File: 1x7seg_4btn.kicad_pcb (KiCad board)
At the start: 2 copper layers, 53.7 x 26.3 mm, 49 parts, among them CON1 AVR-ISP, IC1 ATTINY88-A, Q1 2N7002, Q2 2N7002, Q3 2N7002, U1 74HC14D_653, U10 MC14543B, U2 SW_SPST, U3 SW_SPST, U6 SW_SPST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

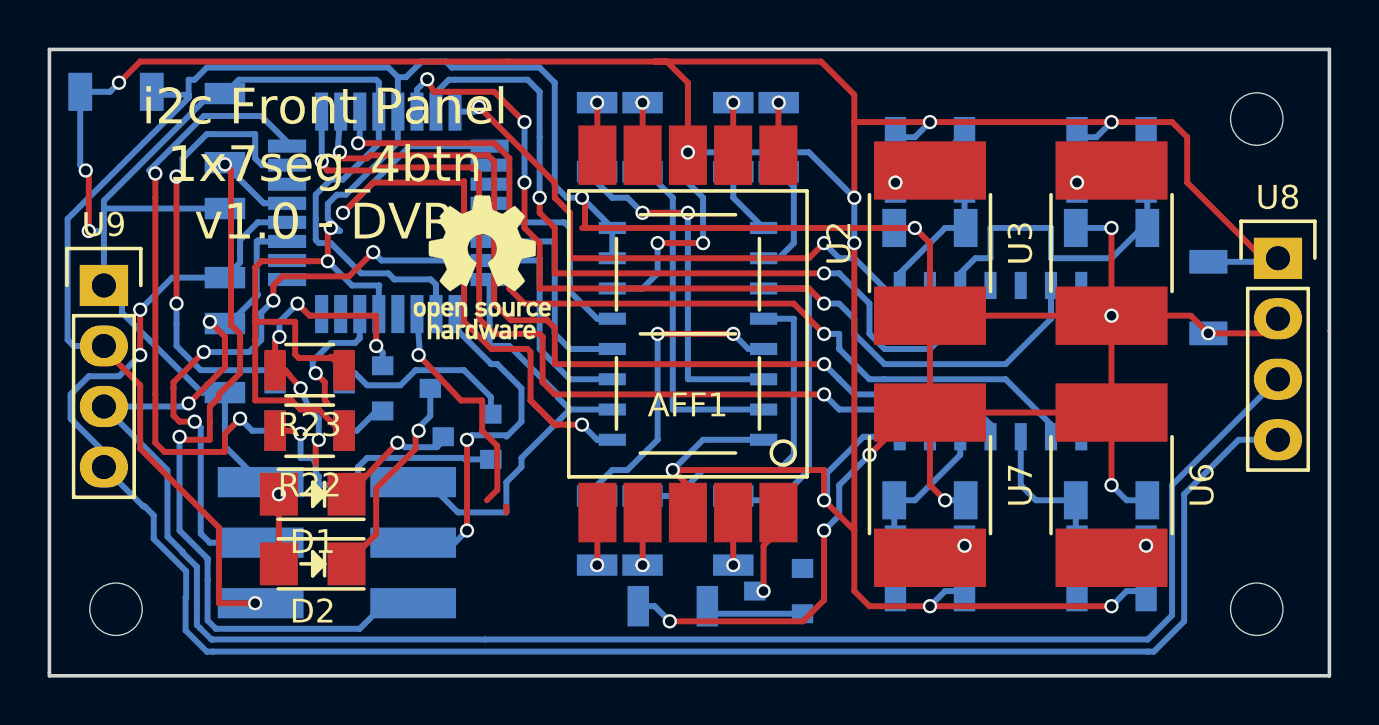
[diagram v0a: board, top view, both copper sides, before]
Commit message: Moved oshw logo
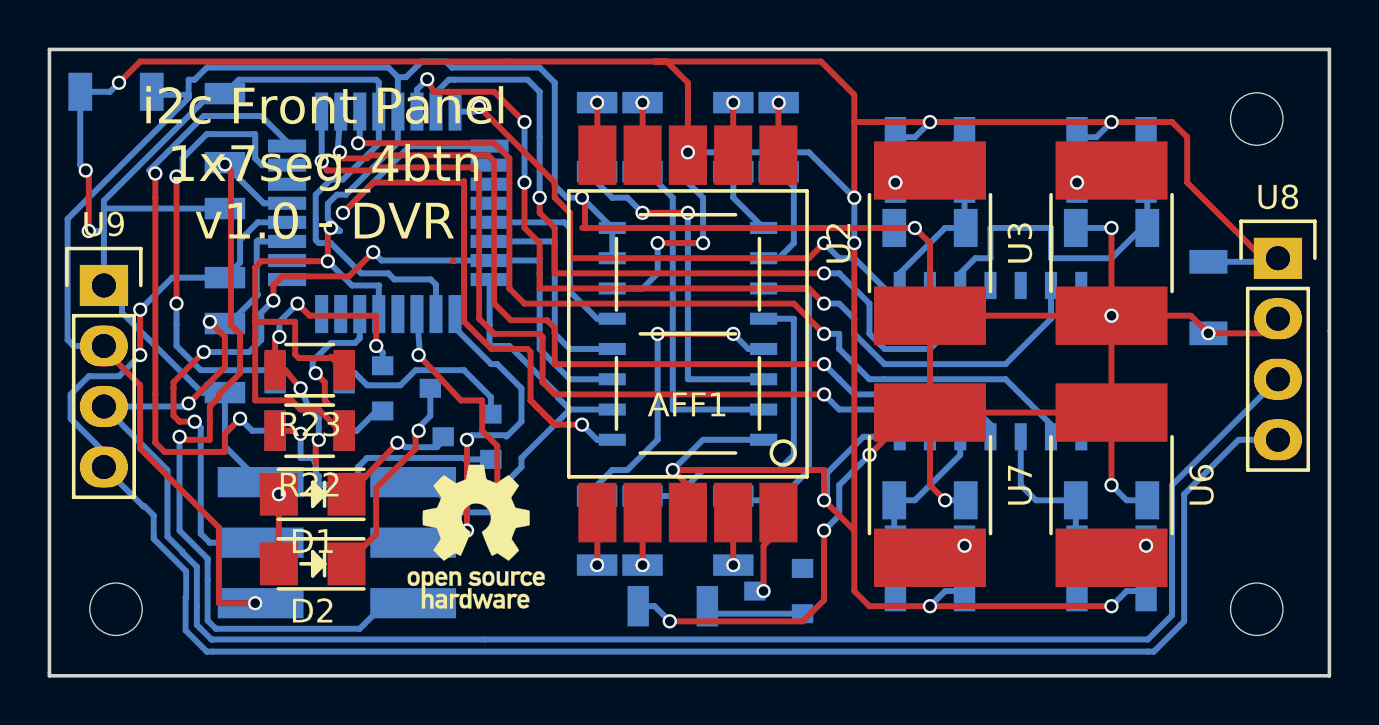
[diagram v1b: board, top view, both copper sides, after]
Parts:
- moved REF*** 11.3 mm to (50.7, 41.5)
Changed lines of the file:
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@@
   )
   (module Symbols:OSHW-Logo_5.7x6mm_SilkScreen (layer F.Cu)
-    (at 50.927 30.226)
+    (at 50.673 41.529)
     (descr "Open Source Hardware Logo")
     (tags "Logo OSHW")

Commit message: Moved header pins on 1x7seg_4btn version to match height on both sides
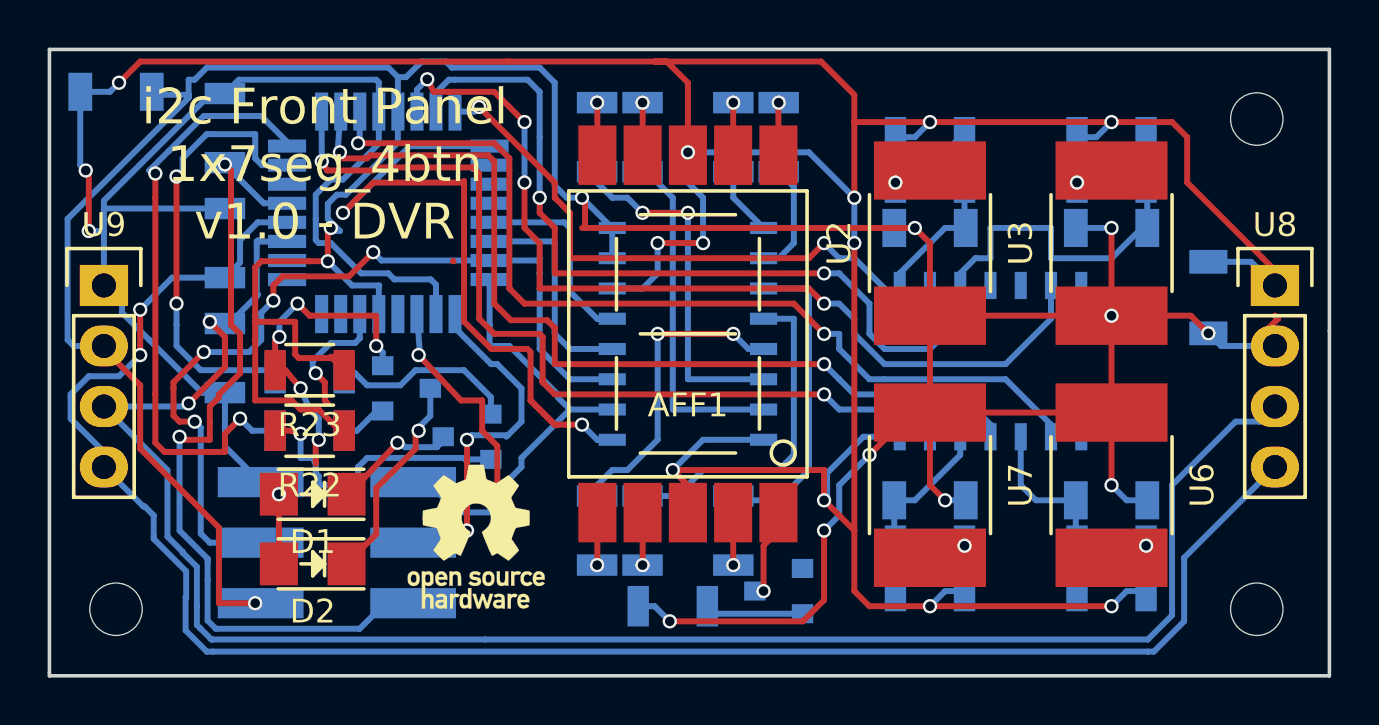
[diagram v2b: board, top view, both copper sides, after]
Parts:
- moved U8 1.15 mm to (84.2, 31.0)
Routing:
- net /SCL: track 78.8 -> 76.6 mm
- net VCC: track 199.8 -> 200.7 mm
- net GND: track 174.8 -> 175.5 mm
- net /SDA: track 78.4 -> 77.8 mm

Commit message: Headers aligned better
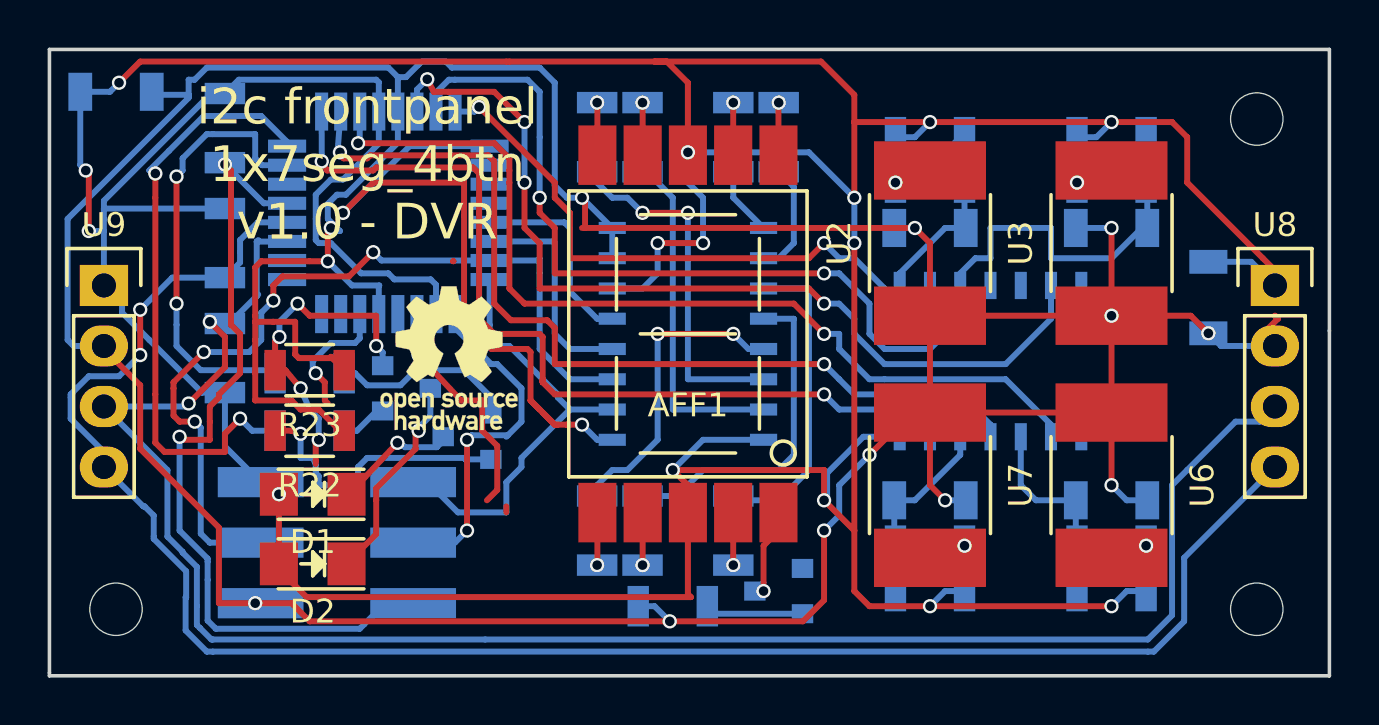
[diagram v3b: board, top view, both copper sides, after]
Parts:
- moved REF*** 7.58 mm to (49.5, 34.0)
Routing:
- net VCC: track 200.7 -> 222.3 mm
- net GND: track 175.5 -> 193.3 mm
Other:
- board text added: "i2c frontpanel 1x7seg_4btn v1.0 - DVR"
- board text removed: "i2c Front Panel 1x7seg_4btn v1.0 - DVR"
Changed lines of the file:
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@@
     (thickness 1.6)
     (drawings 12)
-    (tracks 799)
+    (tracks 807)
     (zones 0)
     (modules 49)
@@
   )
   (module Symbols:OSHW-Logo_5.7x6mm_SilkScreen (layer F.Cu)
-    (at 50.673 41.529)
+    (at 49.53 34.036)
     (descr "Open Source Hardware Logo")
     (tags "Logo OSHW")
@@
     (effects (font (size 1 1) (thickness 0.2)) (justify mirror))
   )
-  (gr_text "i2c Front Panel\n1x7seg_4btn\nv1.0 - DVR" (at 44.323 25.908) (layer F.SilkS)
+  (gr_text "i2c frontpanel\n1x7seg_4btn\nv1.0 - DVR" (at 46.101 25.908) (layer F.SilkS)
     (effects (font (size 1.5 1.5) (thickness 0.3)))
   )
@@
   (segment (start 49.717749 29.969249) (end 49.714998 29.969249) (width 0.25) (layer F.Cu) (net 0))
   (segment (start 49.714998 29.969249) (end 49.717749 29.972) (width 0.25) (layer F.Cu) (net 0))
+  (segment (start 42.39514 42.672) (end 42.39514 42.90314) (width 0.25) (layer F.Cu) (net 1) (status C00000))
+  (segment (start 42.39514 42.90314) (end 43.561 44.069) (width 0.25) (layer F.Cu) (net 1) (status 400000))
+  (segment (start 59.563 43.942) (end 59.563 40.52) (width 0.25) (layer F.Cu) (net 1) (status 800000))
+  (segment (start 59.69 44.069) (end 59.563 43.942) (width 0.25) (layer F.Cu) (net 1))
+  (segment (start 43.561 44.069) (end 59.69 44.069) (width 0.25) (layer F.Cu) (net 1))
   (segment (start 81.407 29.996) (end 83.209 29.996) (width 0.25) (layer B.Cu) (net 1))
   (segment (start 83.209 29.996) (end 84.201 30.988) (width 0.25) (layer B.Cu) (net 1))
@@
   (segment (start 62.738 43.815) (end 62.373 43.815) (width 0.25) (layer B.Cu) (net 9))
   (segment (start 62.738 43.45) (end 62.373 43.815) (width 0.25) (layer B.Cu) (net 9))
+  (segment (start 41.402 44.323) (end 42.926 44.323) (width 0.25) (layer F.Cu) (net 10))
+  (segment (start 43.688 45.085) (end 58.801 45.085) (width 0.25) (layer F.Cu) (net 10))
+  (segment (start 42.926 44.323) (end 43.688 45.085) (width 0.25) (layer F.Cu) (net 10))
   (segment (start 84.201 33.528) (end 81.939 33.528) (width 0.25) (layer B.Cu) (net 10))
   (segment (start 81.939 33.528) (end 81.407 32.996) (width 0.25) (layer B.Cu) (net 10))
@@
   (segment (start 37.187 22.987) (end 37.06 22.86) (width 0.25) (layer B.Cu) (net 10))
   (segment (start 58.801 45.085) (end 64.389 45.085) (width 0.25) (layer F.Cu) (net 10))
+  (segment (start 64.389 45.085) (end 65.278 44.196) (width 0.25) (layer F.Cu) (net 10))
+  (segment (start 65.278 44.196) (end 65.278 41.275) (width 0.25) (layer F.Cu) (net 10))
+  (via (at 65.278 41.275) (size 0.6) (drill 0.4) (layers F.Cu B.Cu) (net 10))
+  (segment (start 67.183 38.1) (end 68.961 36.322) (width 0.25) (layer F.Cu) (net 10))
+  (via (at 67.183 38.1) (size 0.6) (drill 0.4) (layers F.Cu B.Cu) (net 10))
+  (segment (start 65.913 39.37) (end 67.183 38.1) (width 0.25) (layer B.Cu) (net 10))
+  (segment (start 65.913 40.64) (end 65.913 39.37) (width 0.25) (layer B.Cu) (net 10))
   (segment (start 65.278 41.275) (end 65.913 40.64) (width 0.25) (layer B.Cu) (net 10))
-  (segment (start 65.913 40.64) (end 65.913 39.37) (width 0.25) (layer B.Cu) (net 10))
-  (segment (start 65.913 39.37) (end 67.183 38.1) (width 0.25) (layer B.Cu) (net 10))
-  (via (at 67.183 38.1) (size 0.6) (drill 0.4) (layers F.Cu B.Cu) (net 10))
-  (segment (start 67.183 38.1) (end 68.961 36.322) (width 0.25) (layer F.Cu) (net 10))
-  (via (at 65.278 41.275) (size 0.6) (drill 0.4) (layers F.Cu B.Cu) (net 10))
-  (segment (start 65.278 44.196) (end 65.278 41.275) (width 0.25) (layer F.Cu) (net 10))
-  (segment (start 64.389 45.085) (end 65.278 44.196) (width 0.25) (layer F.Cu) (net 10))
   (segment (start 58.166 44.45) (end 57.478 44.45) (width 0.25) (layer B.Cu) (net 10))
+  (via (at 58.801 45.085) (size 0.6) (drill 0.4) (layers F.Cu B.Cu) (net 10))
   (segment (start 58.801 45.085) (end 58.166 44.45) (width 0.25) (layer B.Cu) (net 10))
-  (via (at 58.801 45.085) (size 0.6) (drill 0.4) (layers F.Cu B.Cu) (net 10))
   (segment (start 44.958 28.702) (end 44.704 28.702) (width 0.25) (layer B.Cu) (net 10))
   (segment (start 47.39 24.998602) (end 45.210602 27.178) (width 0.25) (layer B.Cu) (net 10))
